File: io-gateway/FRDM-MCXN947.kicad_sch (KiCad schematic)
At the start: 1 part

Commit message: update mcu lib
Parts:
- removed MCU1: ~, FRDM-MCXN947:FRDM-MCXN947, symbol FRDM-MCXN947__Shield_Template-altium-import:root_0_mirrored_SSQ-108-03-T-D
- added FRDM_MCXN947_1: MCU1, FRDM-MCXN947:FRDM-MCXN947, symbol FRDM-MCXN947__Shield_Template-altium-import:MCU**

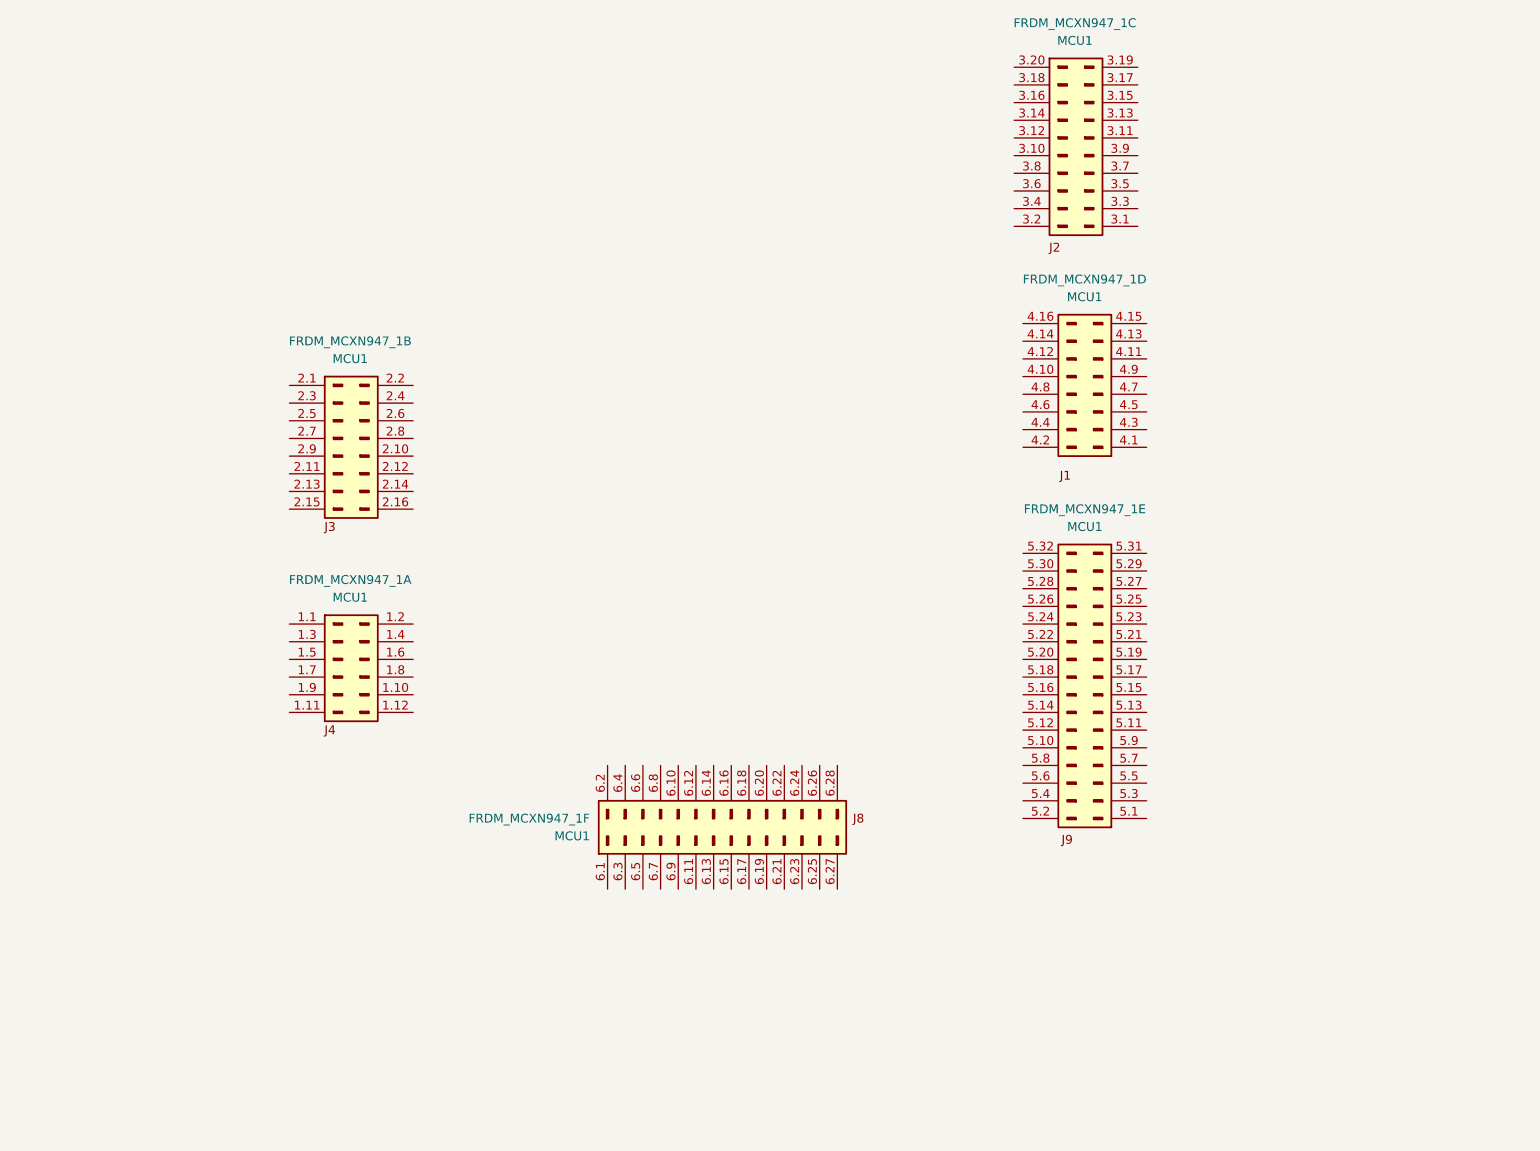
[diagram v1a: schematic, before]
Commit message: Place Relays
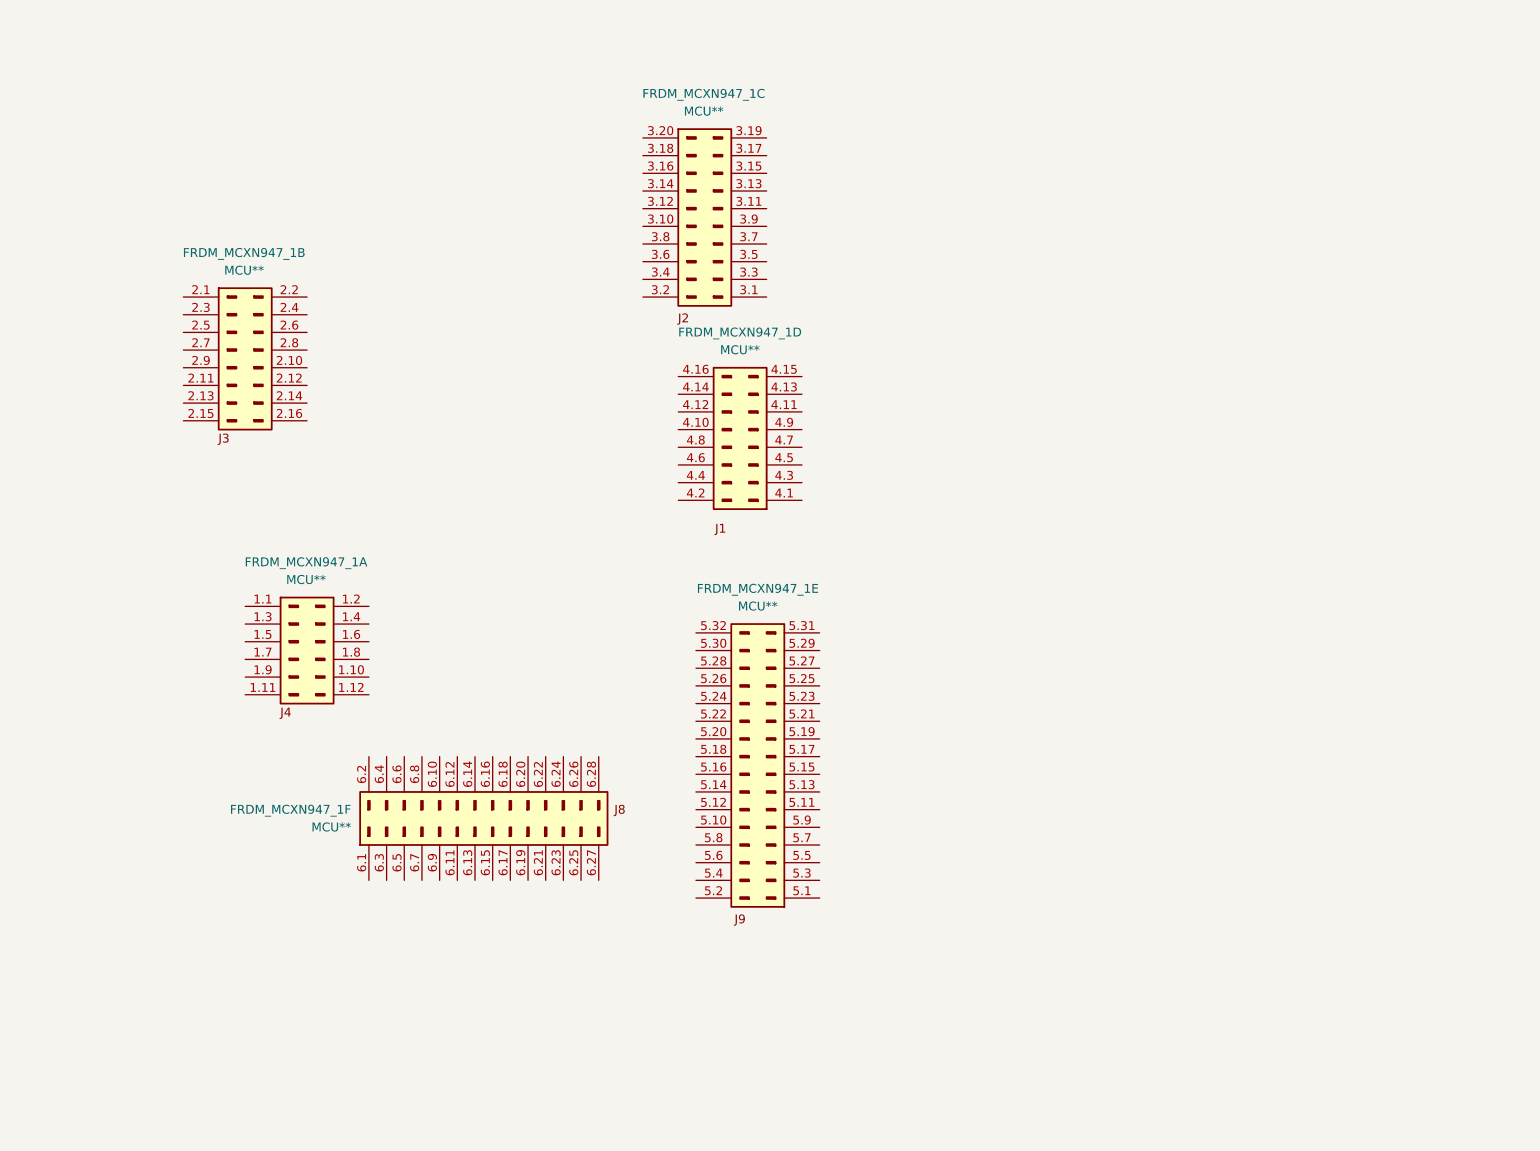
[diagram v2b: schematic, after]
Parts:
- FRDM_MCXN947_1: value MCU1 -> MCU**

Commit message: update
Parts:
- added FRDM_MCXA153_1: MCU**, FFRDM-MCXA153:FRDM-MCXA153-SMD, symbol FRDM_MCXA153:MCU**
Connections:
- new net PWM_DIM1: FRDM_MCXA153_1.1.8 (Pin_J1_8)
- new net RS485_RTS: FRDM_MCXA153_1.1.12 (Pin_J1_12)
- new net RS485_RX: FRDM_MCXA153_1.1.2 (Pin_J1_2)
- new net RS485_TX: FRDM_MCXA153_1.1.4 (Pin_J1_4)
- new net RelayCtrl_K1: FRDM_MCXA153_1.1.6 (Pin_J1_6)
- new net RelayCtrl_K2: FRDM_MCXA153_1.1.10 (Pin_J1_10)

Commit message: layout for first dimmer
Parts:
- removed FRDM_MCXN947_1: MCU**, FRDM-MCXN947:FRDM-MCXN947, symbol FRDM-MCXN947__Shield_Template-altium-import:MCU**
- FRDM_MCXA153_1: now in the parts list

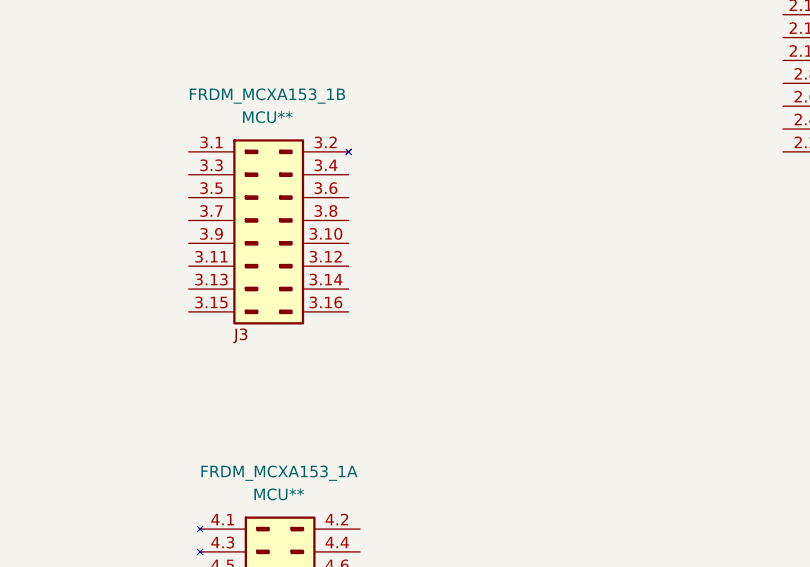
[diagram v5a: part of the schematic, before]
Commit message: fix some drc issues
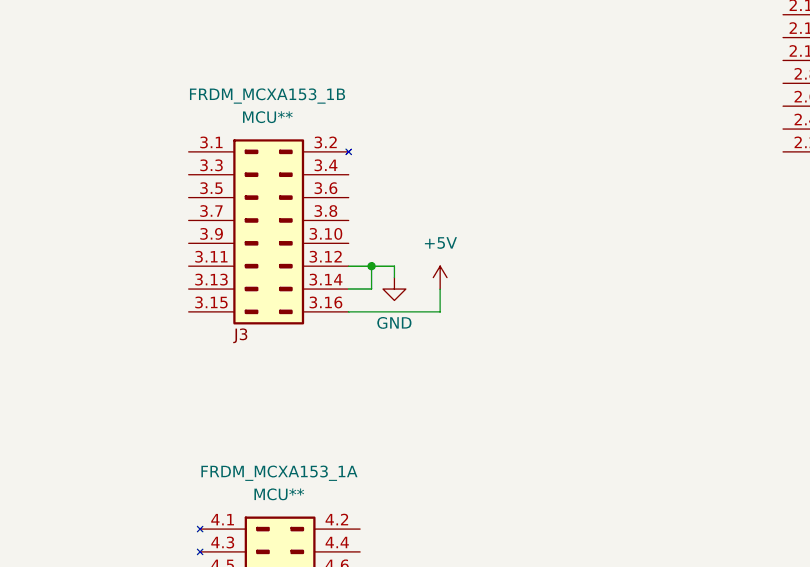
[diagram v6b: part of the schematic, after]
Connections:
- net GND: now reaches FRDM_MCXA153_1.3.12 (Pin_J3_12_GND)
- net GND: now also FRDM_MCXA153_1.3.14 (Pin_J3_14_GND)
- net +5V: now reaches FRDM_MCXA153_1.3.16 (Pin_J3_16_VIN)
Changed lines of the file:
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@@
 	(generator_version "9.0")
 	(paper "A4")
+	(junction
+		(at 195.58 90.17)
+		(diameter 0)
+		(color 0 0 0 0)
+	)
 	(wire
 		(pts
@@
 	(wire
 		(pts
+			(xy 203.2 95.25) (xy 193.04 95.25)
+		)
+		(stroke
+			(width 0)
+			(type default)
+		)
+	)
+	(wire
+		(pts
 			(xy 76.2 162.56) (xy 85.09 162.56)
 		)
@@
 	(wire
 		(pts
+			(xy 198.12 90.17) (xy 195.58 90.17)
+		)
+		(stroke
+			(width 0)
+			(type default)
+		)
+	)
+	(wire
+		(pts
+			(xy 203.2 92.71) (xy 203.2 95.25)
+		)
+		(stroke
+			(width 0)
+			(type default)
+		)
+	)
+	(wire
+		(pts
 			(xy 76.2 165.1) (xy 85.09 165.1)
 		)
@@
 	(wire
 		(pts
+			(xy 193.04 92.71) (xy 195.58 92.71)
+		)
+		(stroke
+			(width 0)
+			(type default)
+		)
+	)
+	(wire
+		(pts
+			(xy 195.58 92.71) (xy 195.58 90.17)
+		)
+		(stroke
+			(width 0)
+			(type default)
+		)
+	)
+	(wire
+		(pts
 			(xy 76.2 157.48) (xy 85.09 157.48)
 		)
@@
 		(pts
 			(xy 76.2 154.94) (xy 85.09 154.94)
+		)
+		(stroke
+			(width 0)
+			(type default)
+		)
+	)
+	(wire
+		(pts
+			(xy 198.12 91.44) (xy 198.12 90.17)
+		)
+		(stroke
+			(width 0)
+			(type default)
+		)
+	)
+	(wire
+		(pts
+			(xy 195.58 90.17) (xy 193.04 90.17)
 		)
 		(stroke
@@
 				(justify right)
 				(hide yes)
+			)
+		)
+	)
+	(symbol
+		(lib_id "power:GND")
+		(at 198.12 91.44 0)
+		(unit 1)
+		(exclude_from_sim no)
+		(in_bom yes)
+		(on_board yes)
+		(dnp no)
+		(fields_autoplaced yes)
+		(property "Reference" "#PWR034"
+			(at 198.12 97.79 0)
+			(effects
+				(font
+					(size 1.27 1.27)
+				)
+				(hide yes)
+			)
+		)
+		(property "Value" "GND"
+			(at 198.12 96.52 0)
+			(effects
+				(font
+					(size 1.27 1.27)
+				)
+			)
+		)
+		(property "Footprint" ""
+			(at 198.12 91.44 0)
+			(effects
+				(font
+					(size 1.27 1.27)
+				)
+				(hide yes)
+			)
+		)
+		(property "Datasheet" ""
+			(at 198.12 91.44 0)
+			(effects
+				(font
+					(size 1.27 1.27)
+				)
+				(hide yes)
+			)
+		)
+		(property "Description" "Power symbol creates a global label with name \"GND\" , ground"
+			(at 198.12 91.44 0)
+			(effects
+				(font
+					(size 1.27 1.27)
+				)
+				(hide yes)
+			)
+		)
+		(pin "1"
+		)
+		(instances
+			(project ""
+				(path "/2cb6f94b-272a-4ed7-b08d-c3630bda6156/f7918fcf-9688-4ae8-a1d7-cb892536f0d4"
+					(reference "#PWR034")
+					(unit 1)
+				)
 			)
 		)
@@
 				)
 			)
+		)
+	)
+	(symbol
+		(lib_id "power:+5V")
+		(at 203.2 92.71 0)
+		(unit 1)
+		(exclude_from_sim no)
+		(in_bom yes)
+		(on_board yes)
+		(dnp no)
+		(fields_autoplaced yes)
+		(property "Reference" "#PWR033"
+			(at 203.2 96.52 0)
+			(effects
+				(font
+					(size 1.27 1.27)
+				)
+				(hide yes)
+			)
+		)
+		(property "Value" "+5V"
+			(at 203.2 87.63 0)
+			(effects
+				(font
+					(size 1.27 1.27)
+				)
+			)
+		)
+		(property "Footprint" ""
+			(at 203.2 92.71 0)
+			(effects
+				(font
+					(size 1.27 1.27)
+				)
+				(hide yes)
+			)
+		)
+		(property "Datasheet" ""
+			(at 203.2 92.71 0)
+			(effects
+				(font
+					(size 1.27 1.27)
+				)
+				(hide yes)
+			)
+		)
+		(property "Description" "Power symbol creates a global label with name \"+5V\""
+			(at 203.2 92.71 0)
+			(effects
+				(font
+					(size 1.27 1.27)
+				)
+				(hide yes)
+			)
+		)
+		(pin "1"
+		)
+		(instances
+			(project ""
+				(path "/2cb6f94b-272a-4ed7-b08d-c3630bda6156/f7918fcf-9688-4ae8-a1d7-cb892536f0d4"
+					(reference "#PWR033")
+					(unit 1)
+				)
+			)

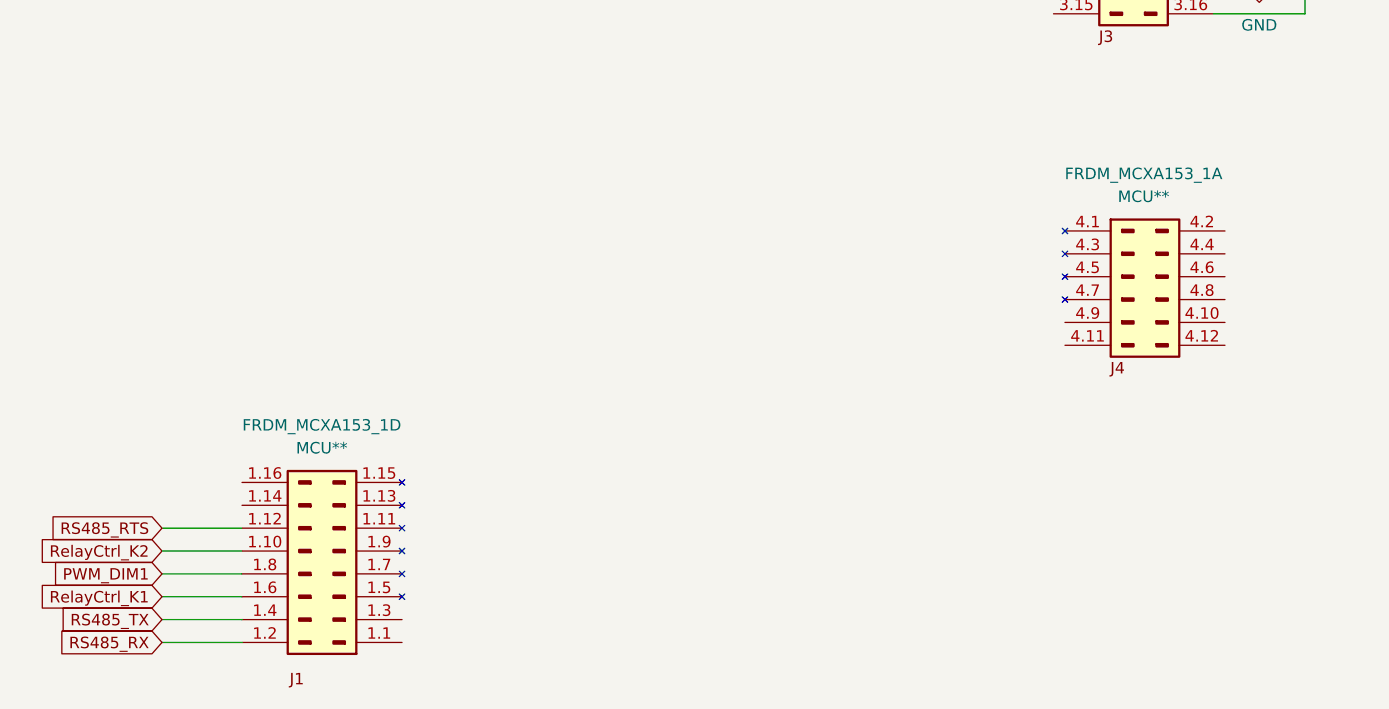
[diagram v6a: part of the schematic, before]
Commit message: Change Holes to Vias
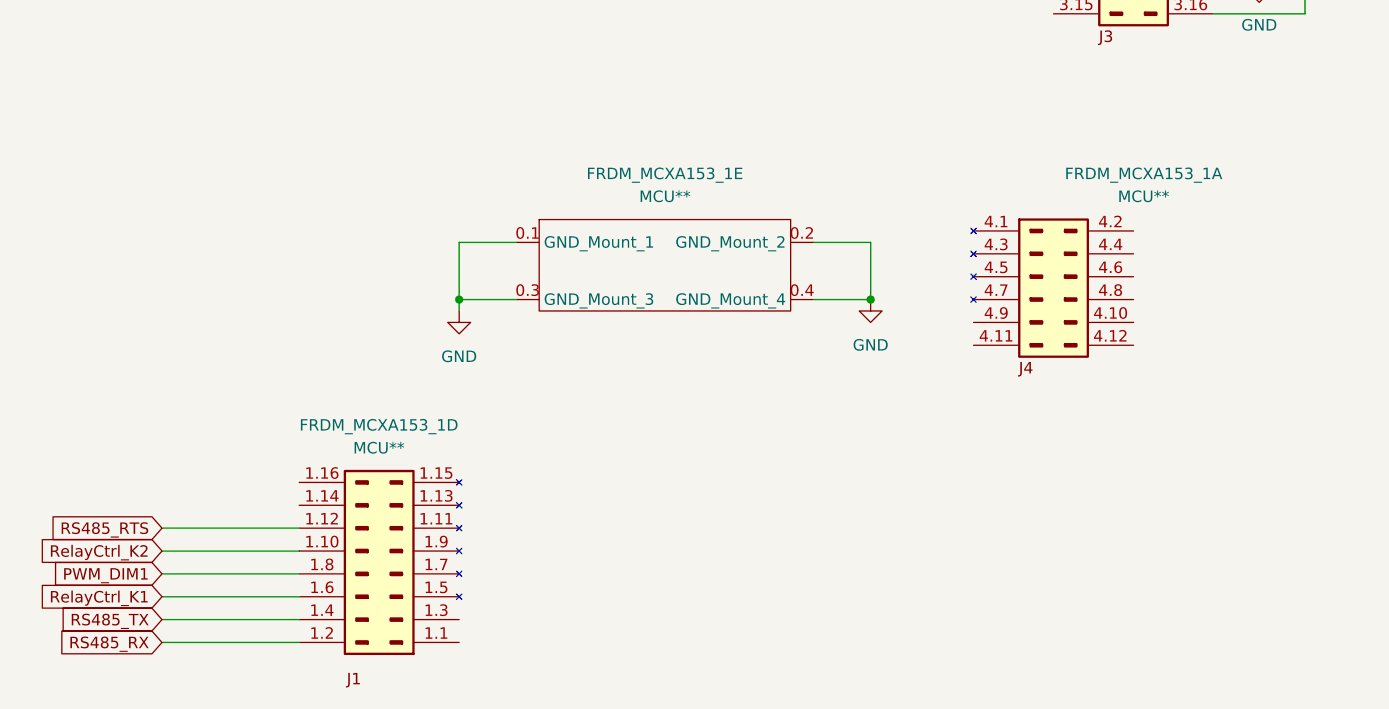
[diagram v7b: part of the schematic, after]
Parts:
- added unit 5 of FRDM_MCXA153_1
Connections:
- net GND: now also FRDM_MCXA153_1.0.1 (GND_Mount_1), FRDM_MCXA153_1.0.2 (GND_Mount_2), FRDM_MCXA153_1.0.3 (GND_Mount_3), FRDM_MCXA153_1.0.4 (GND_Mount_4)
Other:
- moved on the sheet: FRDM_MCXA153_1A, FRDM_MCXA153_1D
